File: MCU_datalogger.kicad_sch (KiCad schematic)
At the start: 0 parts

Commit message: placed schematic parts
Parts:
- added BT1: Battery, symbol Device:Battery
- added C1, C2, C3, C4: C, symbol Device:C
- added C5: C_Polarized, symbol Device:C_Polarized
- added D1, D2: LED, symbol Device:LED
- added H1, H2, H3, H4: MountingHole, symbol Mechanical:MountingHole
- added R1, R2, R3, R4, R5, R6, R7: R, symbol Device:R
- added U1, U2: 24LC1025, symbol Memory_EEPROM:24LC1025
- added U3: DS1337S_, DS1337S_:SOIC127P600X175-8N, symbol downloaded:DS1337S_
- added U4: ATMEGA328P-AU, ATMEGA328P-AU:QFP80P900X900X120-32N, symbol downloaded:ATMEGA328P-AU
- added Y1, Y2: Crystal, symbol Device:Crystal
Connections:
- new net GND: U4.21 (GND), U4.3 (GND), U4.5 (GND)
- new net VCC: U4.4 (VCC), U4.6 (VCC)
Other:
- added sheet connectors (connectors.kicad_sch)
- title: (none) -> ${project_name}

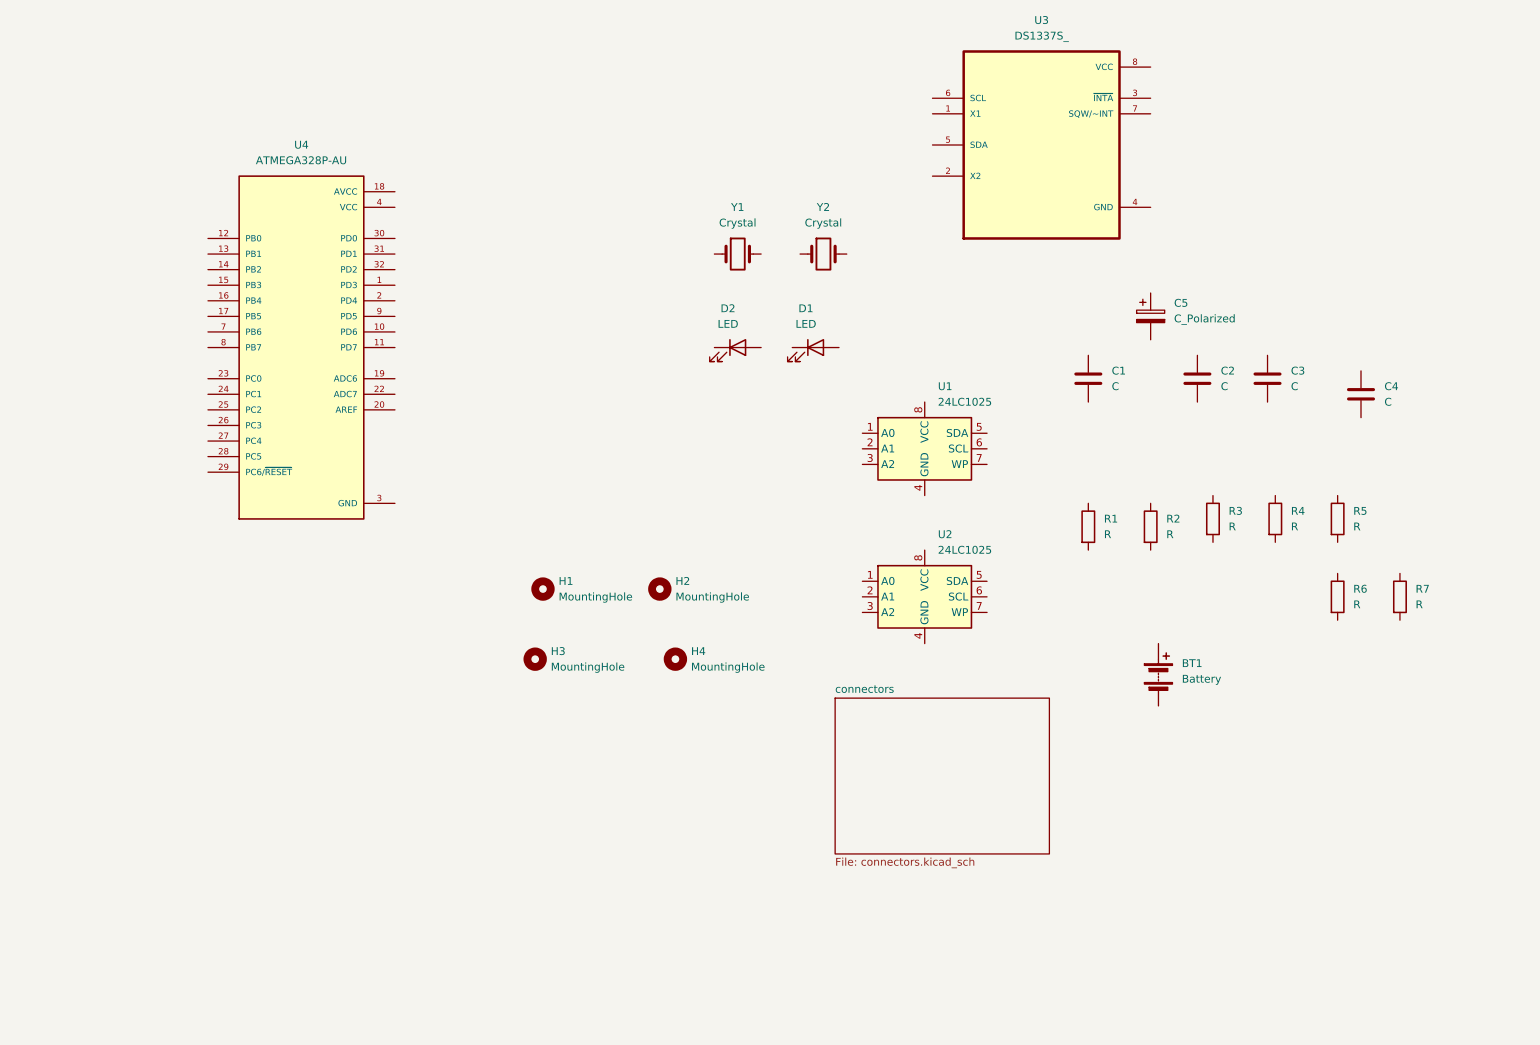
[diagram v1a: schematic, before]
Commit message: assigned footpints in schematic
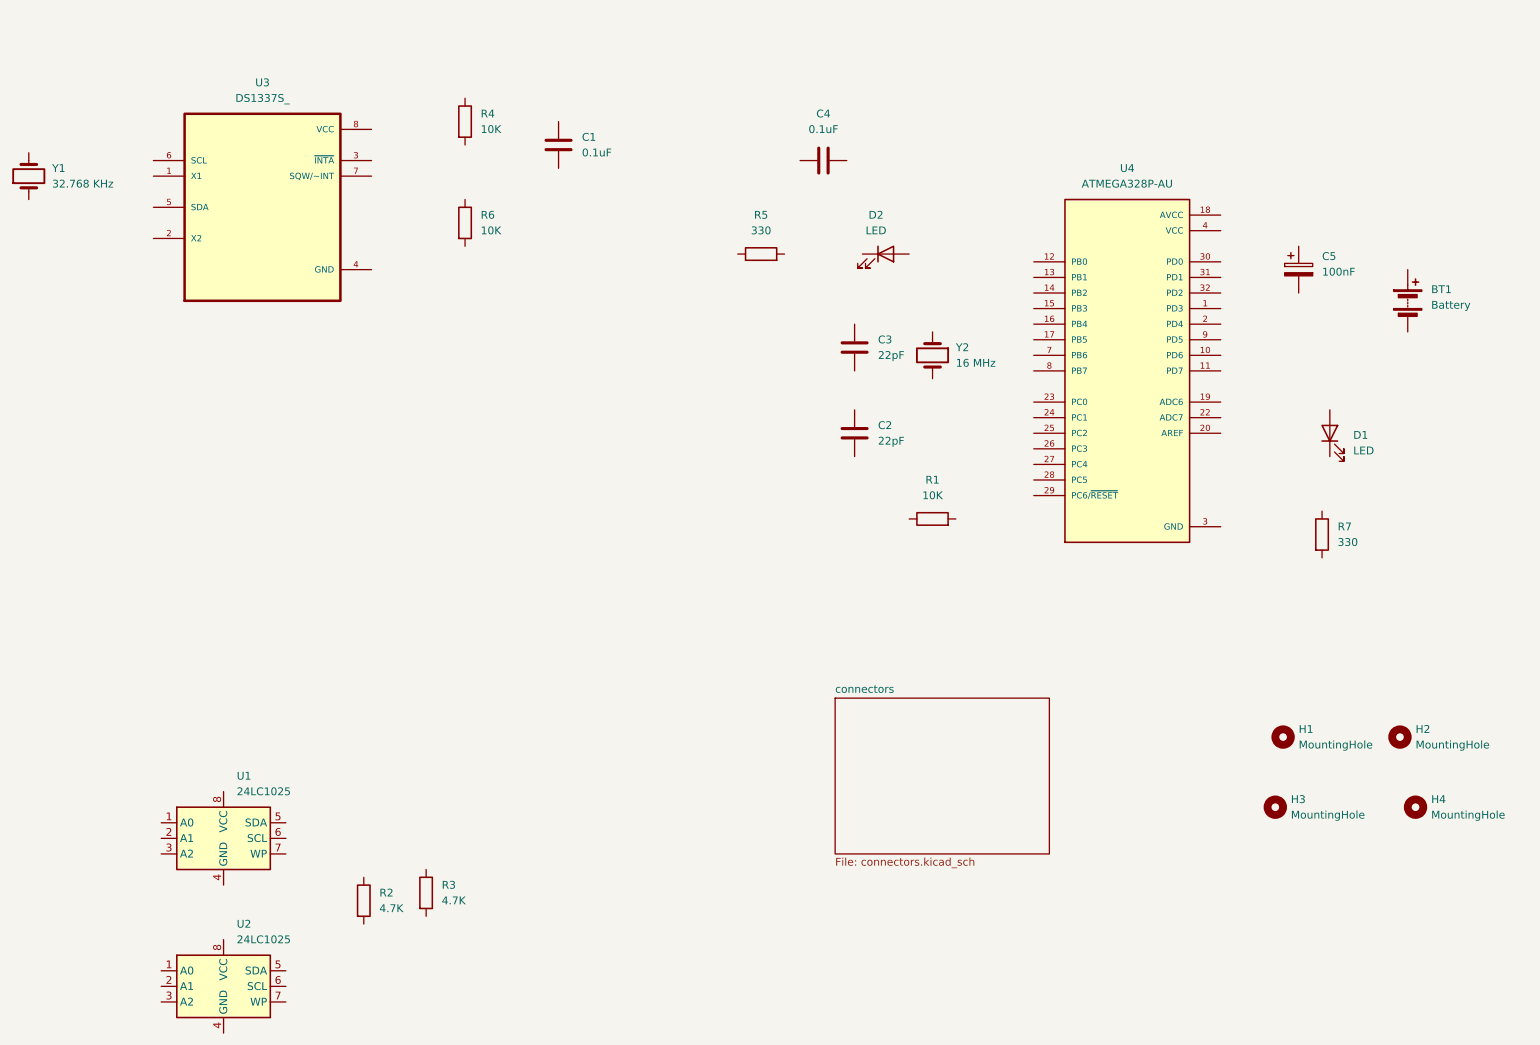
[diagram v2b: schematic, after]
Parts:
- BT1: footprint (none) -> Connector_PinHeader_2.54mm:PinHeader_1x02_P2.54mm_Vertical
- C1, C4: value C -> 0.1uF; footprint (none) -> Capacitor_SMD:C_0805_2012Metric
- C2, C3: value C -> 22pF; footprint (none) -> Capacitor_SMD:C_0805_2012Metric
- C5: value C_Polarized -> 100nF; footprint (none) -> Capacitor_SMD:C_0805_2012Metric
- D1, D2: footprint (none) -> LED_SMD:LED_0805_2012Metric
- H1, H2, H3, H4: footprint (none) -> MountingHole:MountingHole_2.1mm
- R1, R4, R6: value R -> 10K; footprint (none) -> Resistor_SMD:R_0805_2012Metric
- R2, R3: value R -> 4.7K; footprint (none) -> Resistor_SMD:R_0805_2012Metric
- R5, R7: value R -> 330; footprint (none) -> Resistor_SMD:R_0805_2012Metric
- U1, U2: footprint (none) -> downloaded:SOIC-8_5.23x5.23mm_P1.27mm
- U3: footprint DS1337S_:SOIC127P600X175-8N -> downloaded:SOIC127P600X175-8N
- U4: footprint ATMEGA328P-AU:QFP80P900X900X120-32N -> downloaded:QFP80P900X900X120-32N
- Y1: value Crystal -> 32.768 KHz; footprint (none) -> Crystal:Crystal_SMD_5032-2Pin_5.0x3.2mm_HandSoldering
- Y2: value Crystal -> 16 MHz; footprint (none) -> Crystal:Crystal_SMD_5032-2Pin_5.0x3.2mm_HandSoldering
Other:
- moved on the sheet: BT1, C1, C2, C3, C4, C5, D1, D2, H1, H2, H3, H4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
